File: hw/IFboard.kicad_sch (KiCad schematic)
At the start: 99 parts, among them J1 USB_C_Receptacle_USB2.0_16P, J10 IcoTec_36650.2, J11 MC_0,5/_3-G-2,5, J2 Phoenix_1881561, J3 Conn_ARM_SWD_TagConnect_TC203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, J4 Phoenix_1881561, J5 Phoenix_1881561, J6 Phoenix_1881561, J7 IcoTec_36650.2, J8 IcoTec_36650.2, J9 IcoTec_36650.2, SW3 SW_Push, SW4 SW_Push, SW5 SW_Push, SW6 SW_Push, U2 XC6206P332MR-G, U3 TCAN3413DR, U4 ST4E1240DT, U5 MAX232ESE+T, U6 STM32G0B1CBTx, U7 ER_OLEDM0.91_1x-I2C

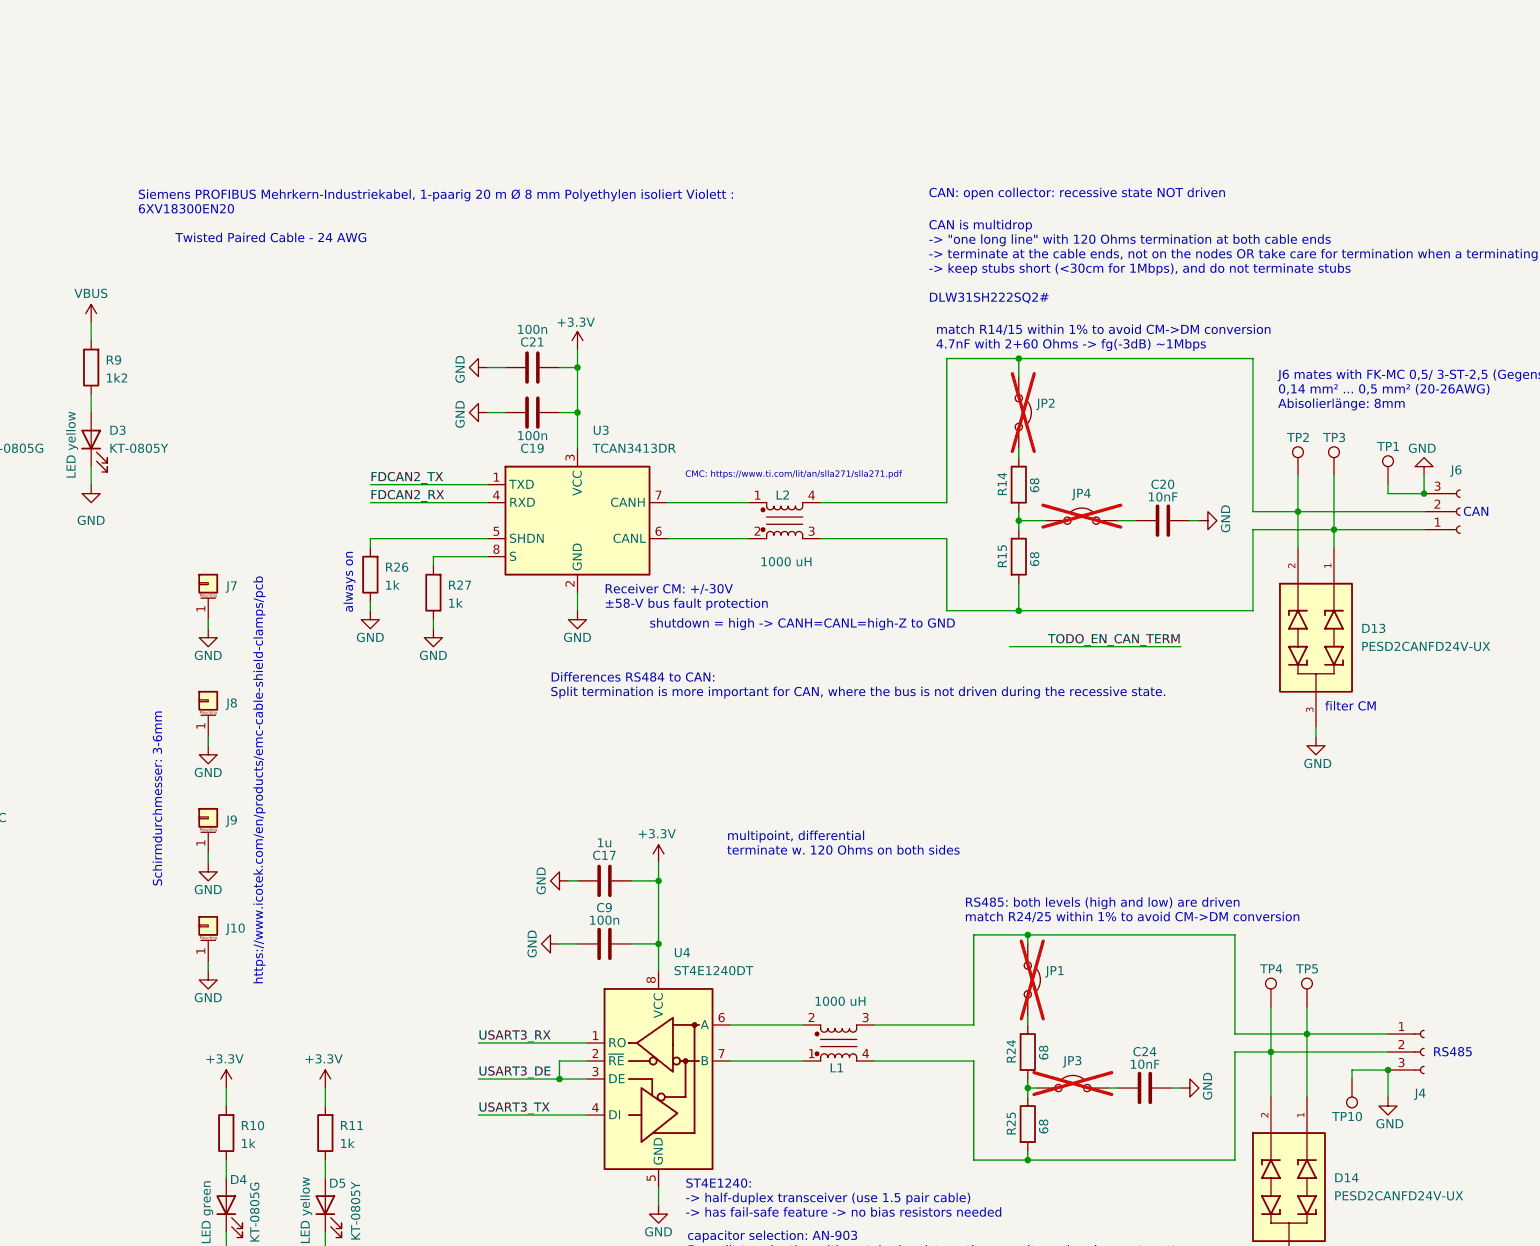
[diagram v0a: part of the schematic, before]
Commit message: added jumpers to be able to short CMCs
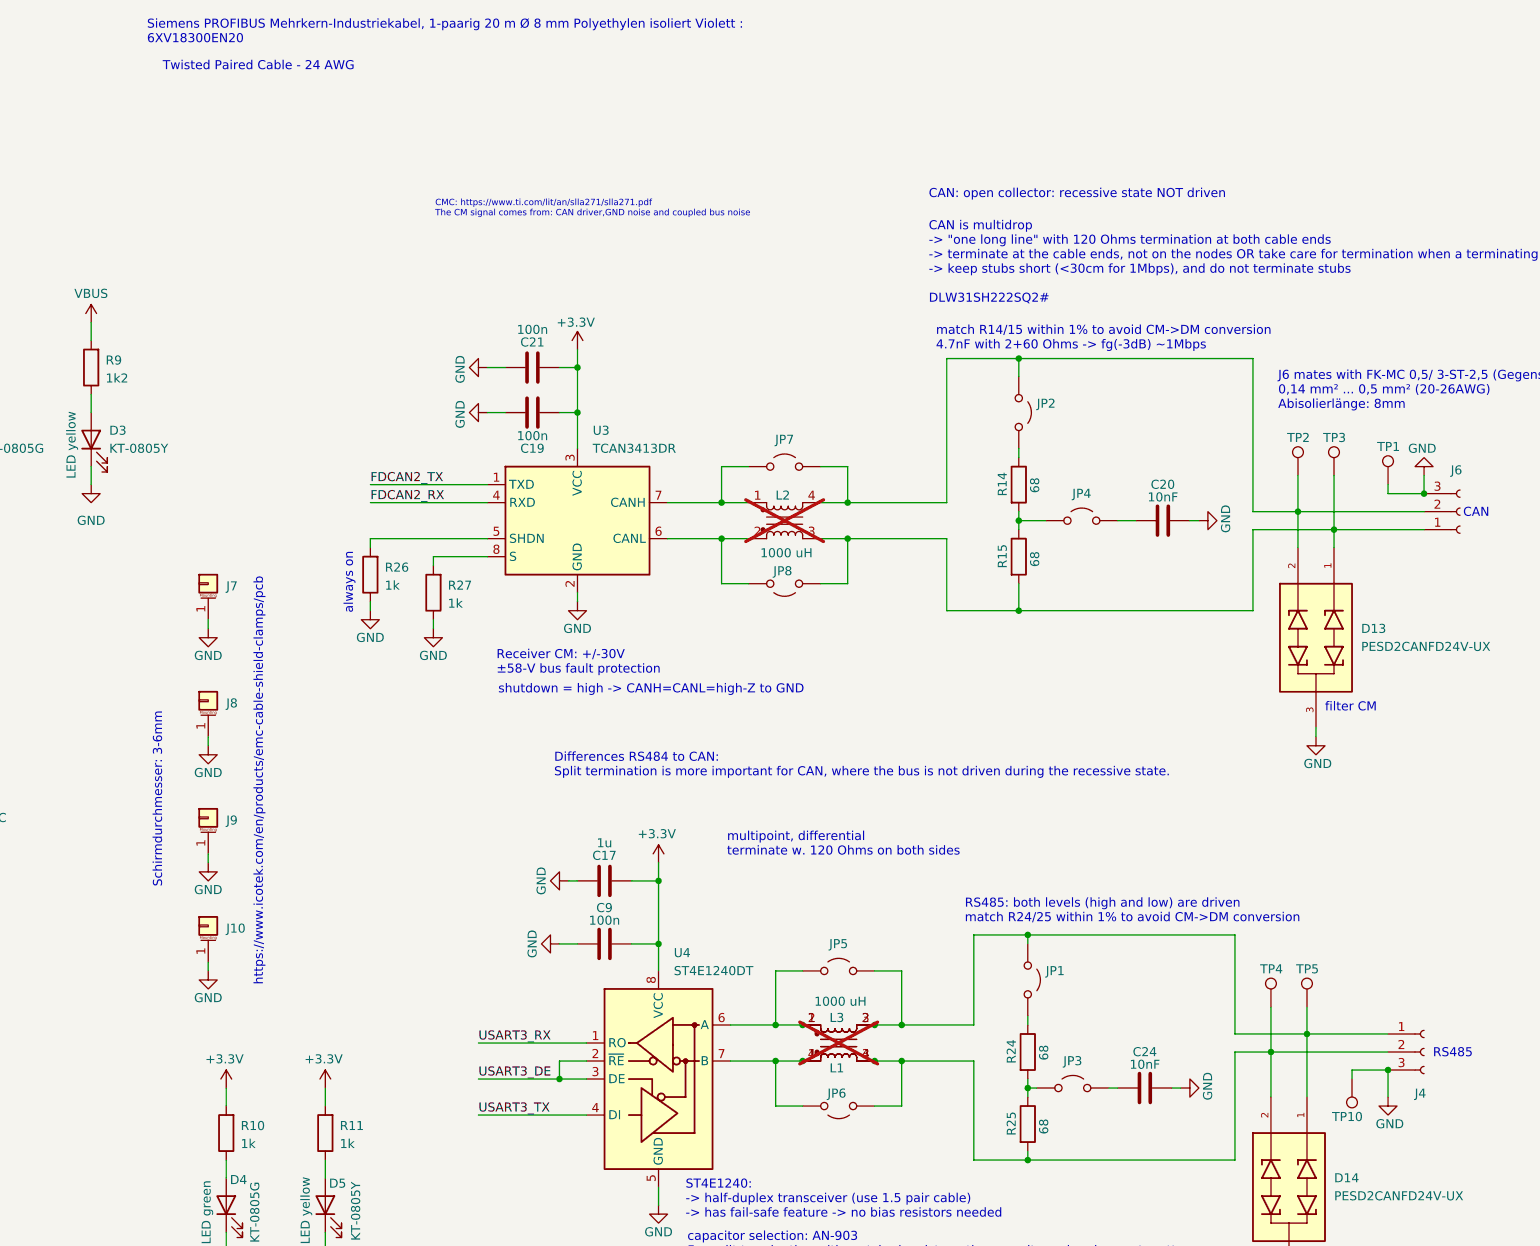
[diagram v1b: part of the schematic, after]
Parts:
- added JP5, JP6, JP7, JP8: Jumper_2_Open, Connector_PinHeader_2.54mm:PinHeader_1x02_P2.54mm_Vertical, symbol Jumper:Jumper_2_Open
- added L3: 100 uH, PZ:L_Wurth_WE-CNSW-1812, symbol PZ:744235101
- JP1, JP2, JP3, JP4: now fitted
- L2: now not fitted
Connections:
- net at L1.2, U4.6 (A): now also JP5.1 (A), L3.1
- net at L1.1, U4.7 (B): now also JP6.2 (B), L3.4
- net at D14.1, J4.1 (Pin_1), JP1.1 (A)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: now also JP5.2 (B), L3.2
- net at D14.2, J4.2 (Pin_2), L1.4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: now also JP6.1 (A), L3.3
- net at D13.2, J6.2 (Pin_2), JP2.1 (A)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: now also JP7.2 (B)
- net at D13.1, J6.1 (Pin_1), L2.3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: now also JP8.1 (A)
- net at L2.2, U3.6 (CANL): now also JP8.2 (B)
- net at L2.1, U3.7 (CANH): now also JP7.1 (A)
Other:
- note added: "CMC: https://www.ti.com/lit/an/slla271/slla271.pdf The CM signal comes from: CAN driver,GND noise and coupled bus noise"
- note removed: "CMC: https://www.ti.com/lit/an/slla271/slla271.pdf"

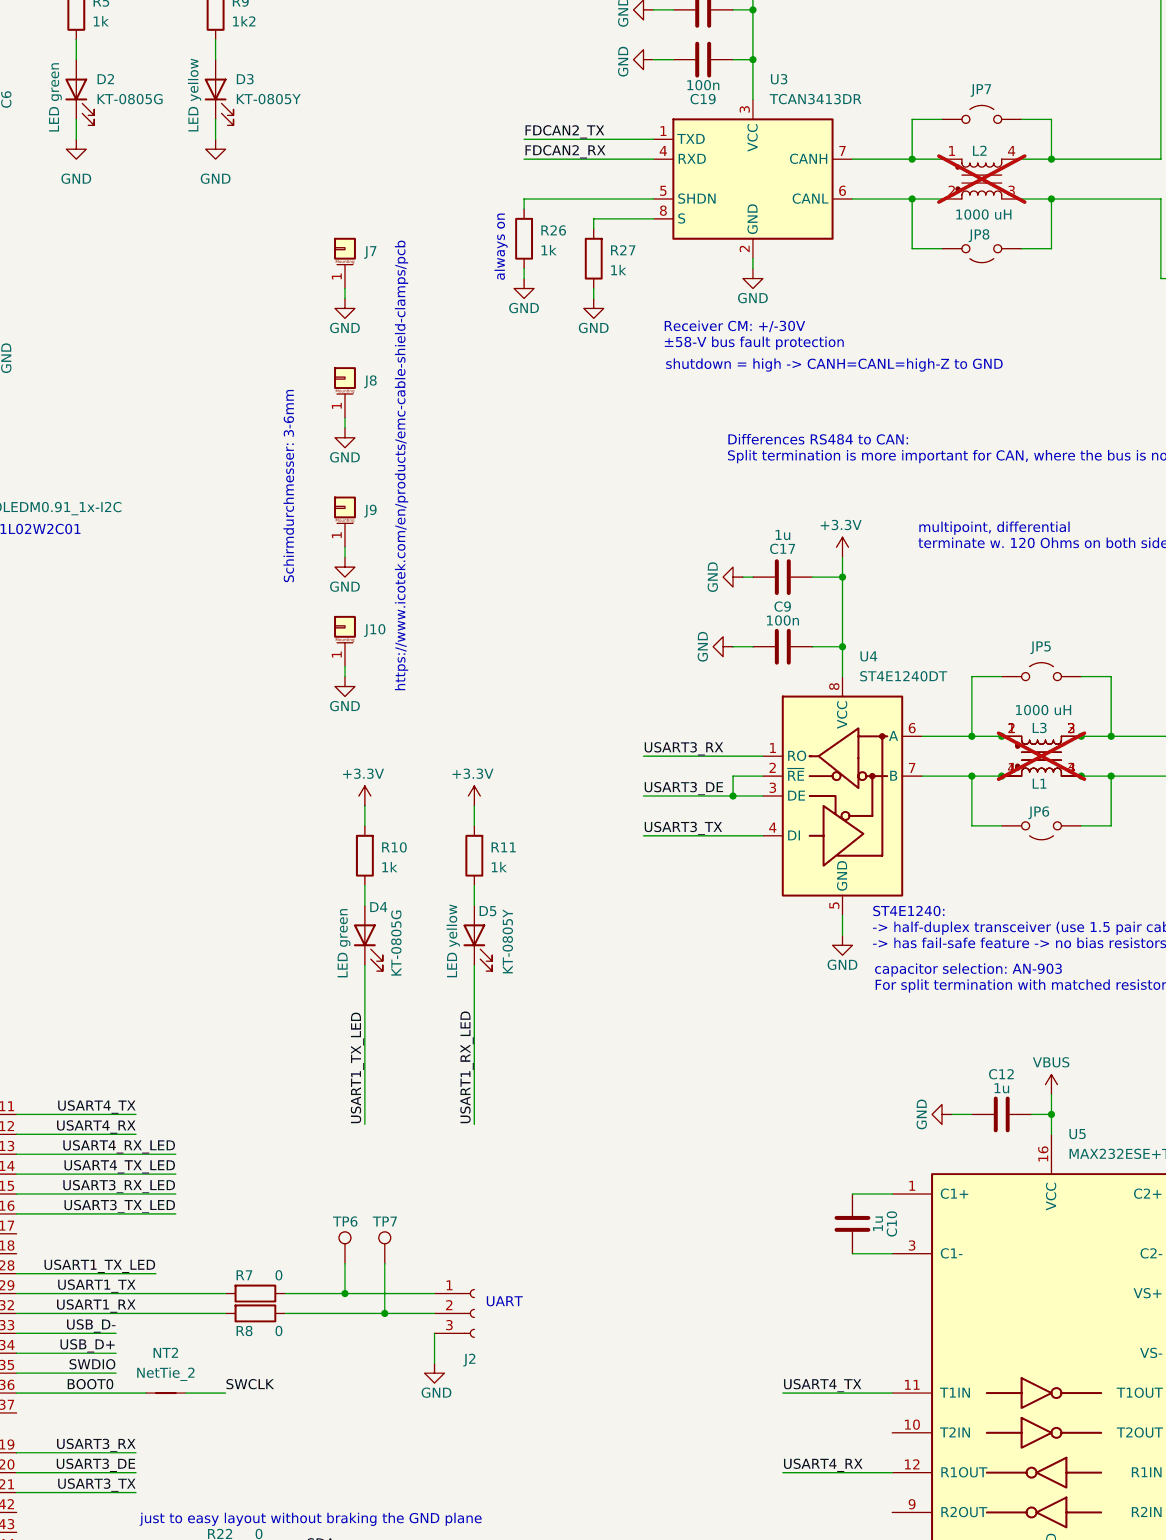
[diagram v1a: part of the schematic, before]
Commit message: corrected rotation offsets for JLC
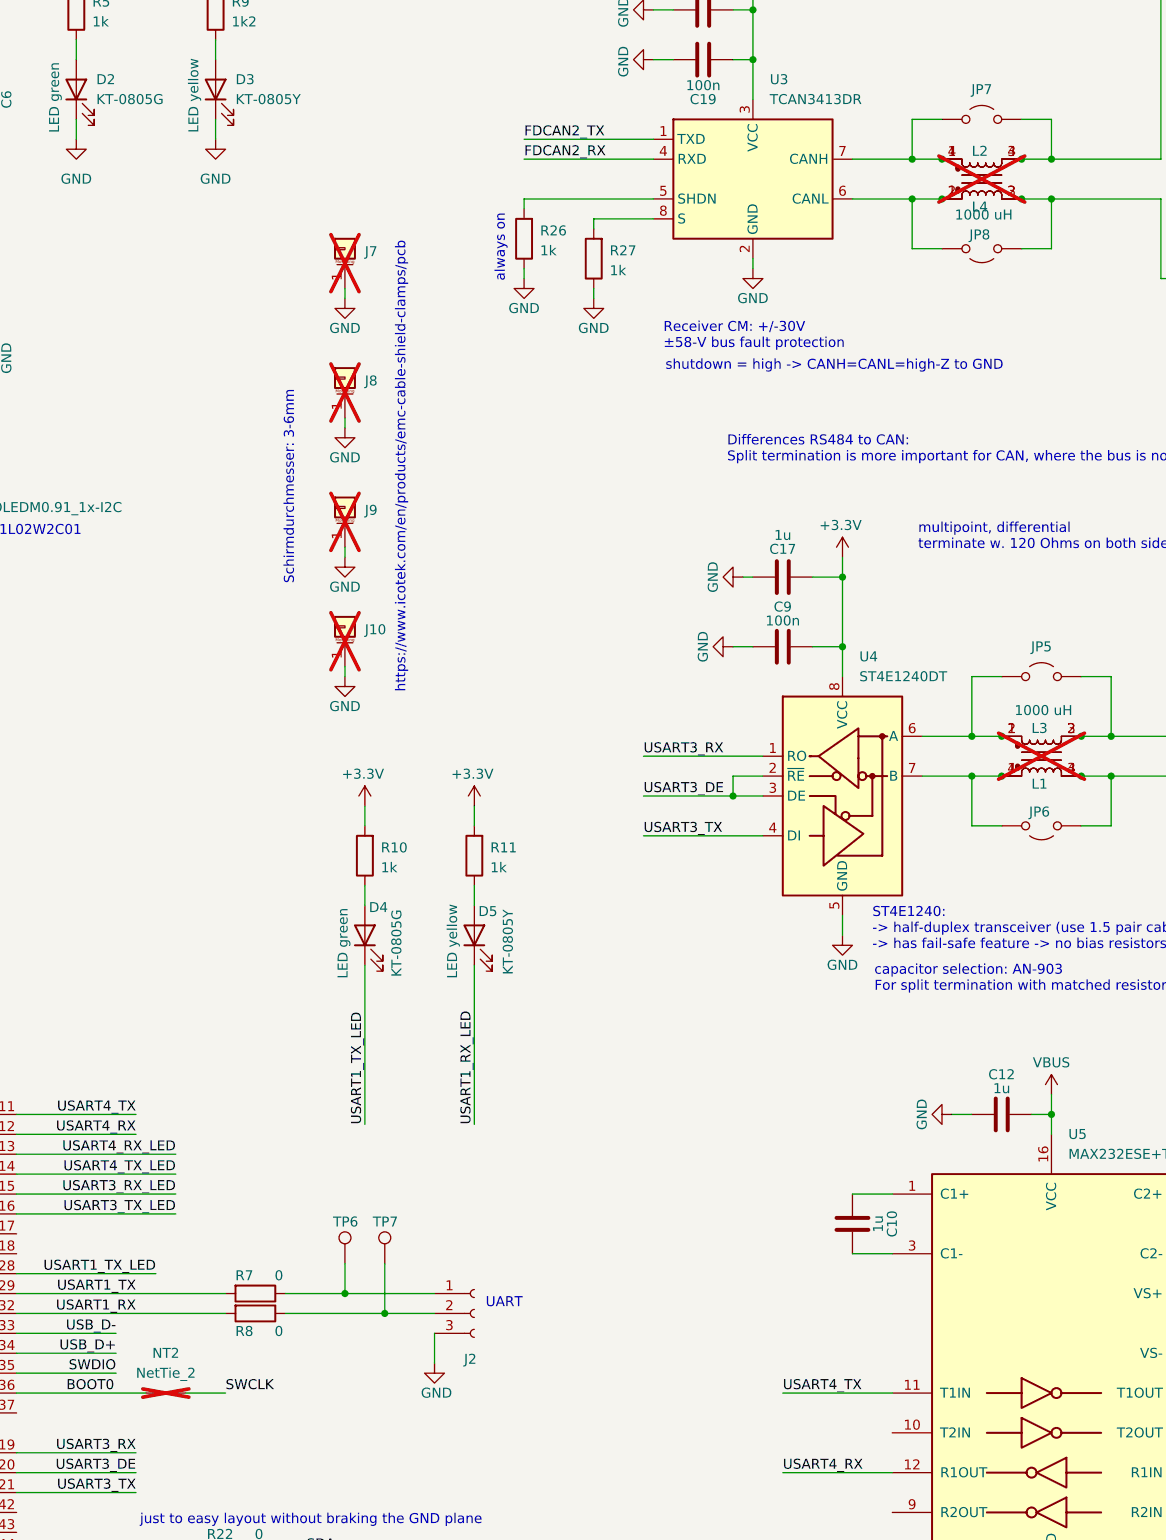
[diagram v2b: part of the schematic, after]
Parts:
- added L4: 100 uH, PZ:L_Wurth_WE-CNSW-1812, symbol PZ:744235101
- J10, J7, J8, J9, L1: now not fitted
- J2, J4, J5, J6: FT Rotation Offset (none) -> 180
- JP1, JP2, JP3, JP4, JP5, JP6, JP7, JP8: FT Rotation Offset (none) -> 90; LCSC Part # (none) -> C492401
- L3: FT Rotation Offset (none) -> 90; now fitted
- NT2: now not fitted; now in the parts list
- U7: FT Rotation Offset (none) -> -90
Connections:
- net at JP7.1 (A), L2.1, U3.7 (CANH): now also L4.4
- net at D13.2, J6.2 (Pin_2), JP2.1 (A)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: now also L4.3
- net at D13.1, J6.1 (Pin_1), JP8.1 (A)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: now also L4.2
- net at JP8.2 (B), L2.2, U3.6 (CANL): now also L4.1

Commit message: first version sent to JLC
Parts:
- added BZ1: CPT-9019S-SMT-TR, PZ:Buzzer_CUI_CPT-9019S-SMT, symbol PZ:Buzzer_CPT-9019S
- added C25: 10nF, Capacitor_SMD:C_0402_1005Metric, symbol Device:C
- added C26: 1u, Capacitor_SMD:C_0402_1005Metric, symbol Device:C
- added D15: PESD2CANFD24V-UX, PZ:TVS_PESD2CANFD24V-UX, symbol PZ:PESD2CANFD24V-UX
- added D16, D17: PESD3V3U1UA, Diode_SMD:D_SOD-323, symbol Diode:PESD3V3U1UL
- added Q1: MMBT3904, Package_TO_SOT_SMD:SOT-23, symbol Transistor_BJT:MMBT3904
- added R29: 1k, Resistor_SMD:R_0603_1608Metric, symbol Device:R
- added TP12, TP13, TP14, TP15: TestPoint_Keystone_5019, PZ:TestPoint_Keystone_5019_Miniature, symbol PZ:TestPoint_Keystone_5019
- C20, C24: footprint Capacitor_SMD:C_0402_1005Metric -> Capacitor_SMD:C_0603_1608Metric; LCSC Part # C15195 -> C57112
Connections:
- net GND: now also C26.1, D15.3, D16.2 (A), D17.2 (A), Q1.2 (E), TP12.1, TP13.1, TP14.1, TP15.1
- net USART4_RX_MAX: now also D15.2
- net USART4_TX_MAX: now also D15.1
- net VBUS: now also BZ1.1 (+), C26.2
- net at J2.1 (Pin_1), R7.1, TP6.1: now also D17.1 (K)
- net at J2.2 (Pin_2), R8.1, TP7.1: now also D16.1 (K)
- net BUZZER: now reaches U6.42 (PB3)
- net BUZZER: now also R29.2
- new net: Q1.1 (B), R29.1
- new net: BZ1.2 (-), Q1.3 (C)
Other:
- note added: "CAN is multidrop -> open collector: recessive state NOT driven, therefore split-temrination more important than on RS485 -> "one long line" with 120 Ohms termination at both cable ends -> terminate at the cable ends, not on the nodes OR take care for termination when a terminating node is removed -> keep stubs short (<30cm for 1Mbps), and do not terminate stubs"
- note added: "RS485: both levels (high and low) are driven -> terminate w. 120 Ohms on both sides -> match R24/25 within 1% to avoid CM->DM conversion"
- note added: "just to ease layout without braking the GND plane"
- note removed: "CAN is multidrop -> "one long line" with 120 Ohms termination at both cable ends -> terminate at the cable ends, not on the nodes OR take care for termination when a terminating node is removed -> keep stubs short (<30cm for 1Mbps), and do not terminate stubs DLW31SH222SQ2#"
- note removed: "CAN: open collector: recessive state NOT driven"
- note removed: "Differences RS484 to CAN: Split termination is more important for CAN, where the bus is not driven during the recessive state."
- note removed: "RS485: both levels (high and low) are driven match R24/25 within 1% to avoid CM->DM conversion"
- note removed: "Siemens PROFIBUS Mehrkern-Industriekabel, 1-paarig 20 m Ø 8 mm Polyethylen isoliert Violett : 6XV18300EN20"
- note removed: "Twisted Paired Cable - 24 AWG"
- note removed: "just to easy layout without braking the GND plane"
- note removed: "multipoint, differential terminate w. 120 Ohms on both sides"
- moved on the sheet: C10, C11, C12, C13, C14, J2, J3, J5, J6, TP1, TP11, TP8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
